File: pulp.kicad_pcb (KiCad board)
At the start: 2 copper layers, 25 parts, among them U2 RP2040, X2 ASE-12.0MHz

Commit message: made edits to PWM
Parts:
- added J1: Conn_01x03_Pin, Connector:FanPinHeader_1x03_P2.54mm_Vertical, F.Cu at (83.0, 79.9)
- moved R10 7.69 mm to (66.0, 99.7), turned to 90 degrees
- moved R11 4.09 mm to (70.3, 100.6)
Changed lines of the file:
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@@
   (net 51 "unconnected-(U2-GPIO29_ADC3-Pad41)")
   (net 52 "/RP2040.kicad_sch/QSPI_SS")
+  (net 53 "/3V3")
   (footprint "Resistor_SMD:R_0201_0603Metric" (layer "F.Cu")
     (at 63.59 71.91)
@@
   )
   (footprint "Resistor_SMD:R_0201_0603Metric" (layer "F.Cu")
-    (at 58.42 98.364 -90)
+    (at 66 99.655 90)
     (descr "Resistor SMD 0201 (0603 Metric), square (rectangular) end terminal, IPC_7351 nominal, (Body size source: https://www.vishay.com/docs/20052/crcw0201e3.pdf), generated with kicad-footprint-generator")
     (tags "resistor")
@@
     (fp_line (start 0.3 0.15) (end -0.3 0.15)
       (stroke (width 0.1) (type solid)) (layer "F.Fab"))
-    (pad "" smd roundrect (at -0.345 0 270) (size 0.318 0.36) (layers "F.Paste") (roundrect_rratio 0.25))
-    (pad "" smd roundrect (at 0.345 0 270) (size 0.318 0.36) (layers "F.Paste") (roundrect_rratio 0.25))
-    (pad "1" smd roundrect (at -0.32 0 270) (size 0.46 0.4) (layers "F.Cu" "F.Mask") (roundrect_rratio 0.25)
+    (pad "" smd roundrect (at -0.345 0 90) (size 0.318 0.36) (layers "F.Paste") (roundrect_rratio 0.25))
+    (pad "" smd roundrect (at 0.345 0 90) (size 0.318 0.36) (layers "F.Paste") (roundrect_rratio 0.25))
+    (pad "1" smd roundrect (at -0.32 0 90) (size 0.46 0.4) (layers "F.Cu" "F.Mask") (roundrect_rratio 0.25)
       (net 3 "/RP2040.kicad_sch/3V3") (pintype "passive"))
-    (pad "2" smd roundrect (at 0.32 0 270) (size 0.46 0.4) (layers "F.Cu" "F.Mask") (roundrect_rratio 0.25)
+    (pad "2" smd roundrect (at 0.32 0 90) (size 0.46 0.4) (layers "F.Cu" "F.Mask") (roundrect_rratio 0.25)
       (net 5 "Net-(X2-EN)") (pintype "passive"))
     (model "${KICAD6_3DMODEL_DIR}/Resistor_SMD.3dshapes/R_0201_0603Metric.wrl"
@@
   )
   (footprint "Resistor_SMD:R_0201_0603Metric" (layer "F.Cu")
-    (at 66.228 100.584)
+    (at 70.32 100.584)
     (descr "Resistor SMD 0201 (0603 Metric), square (rectangular) end terminal, IPC_7351 nominal, (Body size source: https://www.vishay.com/docs/20052/crcw0201e3.pdf), generated with kicad-footprint-generator")
     (tags "resistor")
@@
       (net 1 "/RP2040.kicad_sch/~{RST}") (pintype "passive"))
     (model "${KICAD6_3DMODEL_DIR}/Resistor_SMD.3dshapes/R_0201_0603Metric.wrl"
+      (offset (xyz 0 0 0))
+      (scale (xyz 1 1 1))
+      (rotate (xyz 0 0 0))
+    )
+  )
+  (footprint "Connector:FanPinHeader_1x03_P2.54mm_Vertical" (layer "F.Cu")
+    (at 83 79.92 -90)
+    (descr "3-pin CPU fan Through hole pin header, see http://www.formfactors.org/developer%5Cspecs%5Crev1_2_public.pdf")
+    (tags "pin header 3-pin CPU fan")
+    (property "Sheetfile" "pulp.kicad_sch")
+    (property "Sheetname" "")
+    (property "ki_description" "Generic connector, single row, 01x03, script generated")
+    (property "ki_keywords" "connector")
+    (attr through_hole)
+    (fp_text reference "J1" (at 2.5 -3.4 90) (layer "F.SilkS")
+        (effects (font (size 1 1) (thickness 0.15)))
+    )
+    (fp_text value "Conn_01x03_Pin" (at 2.55 4.5 90) (layer "F.Fab")
+        (effects (font (size 1 1) (thickness 0.15)))
+    )
+    (fp_text user "${REFERENCE}" (at 2.45 1.8 90) (layer "F.Fab")
+        (effects (font (size 1 1) (thickness 0.15)))
+    )
+    (fp_line (start -1.35 -2.65) (end 6.45 -2.65)
+      (stroke (width 0.12) (type solid)) (layer "F.SilkS"))
+    (fp_line (start -1.35 3.4) (end -1.35 -2.65)
+      (stroke (width 0.12) (type solid)) (layer "F.SilkS"))
+    (fp_line (start 0 2.29) (end 5.08 2.29)
+      (stroke (width 0.12) (type solid)) (layer "F.SilkS"))
+    (fp_line (start 0 3.3) (end 0 2.29)
+      (stroke (width 0.12) (type solid)) (layer "F.SilkS"))
+    (fp_line (start 5.08 2.29) (end 5.08 3.3)
+      (stroke (width 0.12) (type solid)) (layer "F.SilkS"))
+    (fp_line (start 6.45 -2.65) (end 6.45 3.4)
+      (stroke (width 0.12) (type solid)) (layer "F.SilkS"))
+    (fp_line (start 6.45 3.4) (end -1.35 3.4)
+      (stroke (width 0.12) (type solid)) (layer "F.SilkS"))
+    (fp_line (start -1.75 3.8) (end -1.75 -3.05)
+      (stroke (width 0.05) (type solid)) (layer "F.CrtYd"))
+    (fp_line (start -1.75 3.8) (end 6.85 3.8)
+      (stroke (width 0.05) (type solid)) (layer "F.CrtYd"))
+    (fp_line (start 6.85 -3.05) (end -1.75 -3.05)
+      (stroke (width 0.05) (type solid)) (layer "F.CrtYd"))
+    (fp_line (start 6.85 -3.05) (end 6.85 3.8)
+      (stroke (width 0.05) (type solid)) (layer "F.CrtYd"))
+    (fp_line (start -1.25 -2.55) (end 6.35 -2.55)
+      (stroke (width 0.1) (type solid)) (layer "F.Fab"))
+    (fp_line (start -1.25 3.3) (end -1.25 -2.55)
+      (stroke (width 0.1) (type solid)) (layer "F.Fab"))
+    (fp_line (start 0 2.3) (end 0 3.3)
+      (stroke (width 0.1) (type solid)) (layer "F.Fab"))
+    (fp_line (start 5.05 2.3) (end 0 2.3)
+      (stroke (width 0.1) (type solid)) (layer "F.Fab"))
+    (fp_line (start 5.05 3.3) (end 5.05 2.3)
+      (stroke (width 0.1) (type solid)) (layer "F.Fab"))
+    (fp_line (start 6.35 -2.55) (end 6.35 3.3)
+      (stroke (width 0.1) (type solid)) (layer "F.Fab"))
+    (fp_line (start 6.35 3.3) (end -1.25 3.3)
+      (stroke (width 0.1) (type solid)) (layer "F.Fab"))
+    (pad "1" thru_hole rect (at 0 0) (size 2.03 1.73) (drill 1.02) (layers "*.Cu" "*.Mask")
+      (net 32 "/RP2040.kicad_sch/GPIO14_PWM_RIGHT") (pinfunction "Pin_1") (pintype "passive"))
+    (pad "2" thru_hole oval (at 2.54 0) (size 2.03 1.73) (drill 1.02) (layers "*.Cu" "*.Mask")
+      (net 2 "GND") (pinfunction "Pin_2") (pintype "passive"))
+    (pad "3" thru_hole oval (at 5.08 0) (size 2.03 1.73) (drill 1.02) (layers "*.Cu" "*.Mask")
+      (net 53 "/3V3") (pinfunction "Pin_3") (pintype "passive"))
+    (model "${KICAD6_3DMODEL_DIR}/Connector.3dshapes/FanPinHeader_1x03_P2.54mm_Vertical.wrl"
       (offset (xyz 0 0 0))
       (scale (xyz 1 1 1))
@@
   (gr_rect (start 45.72 40.64) (end 86.36 121.92)
     (stroke (width 0.2) (type default)) (fill none) (layer "F.Cu"))
-  (segment (start 65.874 100.55) (end 65.908 100.584) (width 0.25) (layer "F.Cu") (net 3))
 )

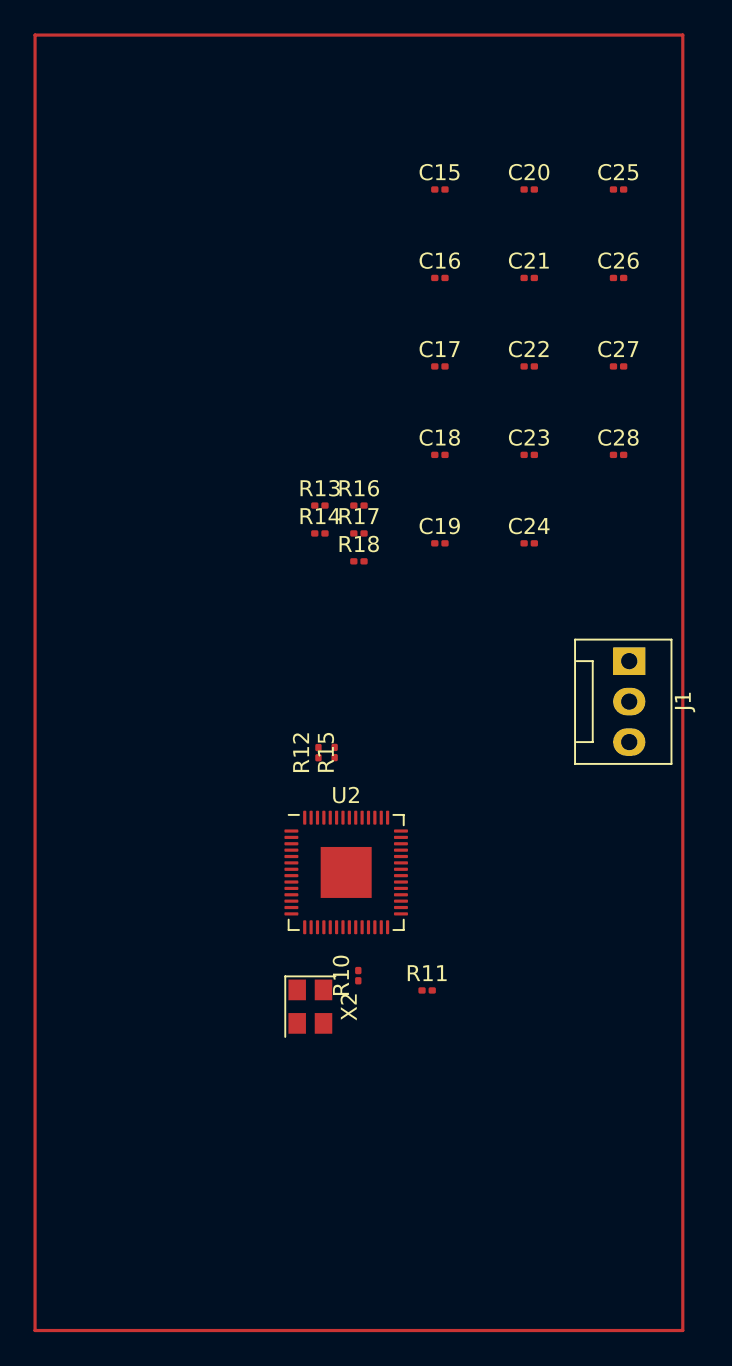
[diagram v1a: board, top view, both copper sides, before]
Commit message: adds QMC5883L
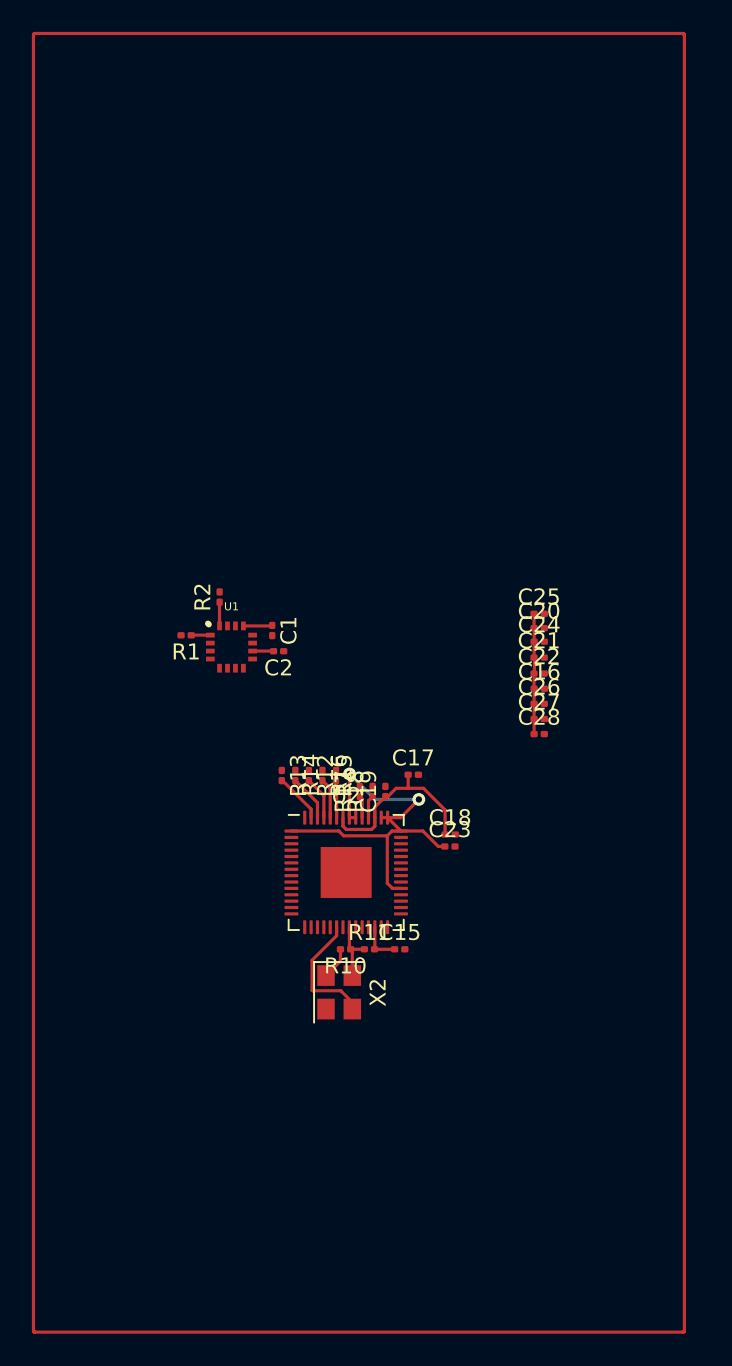
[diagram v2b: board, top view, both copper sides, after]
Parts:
- removed J1: Conn_01x03_Pin, Connector:FanPinHeader_1x03_P2.54mm_Vertical
- added C1: 0.1uF, Capacitor_SMD:C_0201_0603Metric, F.Cu at (60.6, 78.0)
- added C2: 4.7uF, Capacitor_SMD:C_0201_0603Metric, F.Cu at (61.0, 79.3)
- added R1: 4.7K, Resistor_SMD:R_0201_0603Metric, F.Cu at (55.2, 78.3)
- added R2: 4.7K, Resistor_SMD:R_0201_0603Metric, F.Cu at (57.3, 75.9)
- added U1: HMC5883L, Sensor:HMC5883L, F.Cu at (58.0, 79.0)
- moved C15 47.7 mm to (68.6, 98.0)
- moved C20 27.5 mm to (77.3, 77.8)
- moved C26 27.2 mm to (77.3, 82.6)
- moved C25 27.1 mm to (77.3, 77.0)
- moved C16 26.5 mm to (77.4, 81.7)
- moved C17 25.7 mm to (69.5, 87.0)
- moved C23 25.1 mm to (71.8, 91.5)
- moved C18 23.8 mm to (71.8, 90.8)
- moved C21 23.8 mm to (77.3, 79.7)
- moved C27 22.7 mm to (77.3, 83.5)
- moved C22 19.3 mm to (77.3, 80.7)
- moved C28 18.2 mm to (77.3, 84.5)
- moved R13 17.1 mm to (61.2, 87.1), turned to -90 degrees
- moved R16 17.1 mm to (63.8, 87.1), turned to -90 degrees
- moved R17 16.2 mm to (66.1, 88.1), turned to 90 degrees
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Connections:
- U2 pad 32: /RP2040.kicad_sch/I2C 0 SDA -> /QMC5883L/SDA
- U2 pad 34: /RP2040.kicad_sch/I2C 0 SCL -> /QMC5883L/SCL
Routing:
- net /RP2040.kicad_sch/3V3: track 0.00 -> 38.0 mm, vias 0 -> 2
- net /RP2040.kicad_sch/1V1: track 0.00 -> 11.8 mm
- net Net-(U2-XIN): track 0.00 -> 7.86 mm
- net Net-(U2-QSPI_SD1): track 0.00 -> 3.11 mm
- net Net-(U2-QSPI_SD2): track 0.00 -> 2.90 mm
- net Net-(U2-QSPI_SD0): track 0.00 -> 2.71 mm
- net /RP2040.kicad_sch/~{RST}: track 0.00 -> 2.65 mm
- net Net-(U2-QSPI_SCLK): track 0.00 -> 2.53 mm
- net Net-(U2-QSPI_SD3): track 0.00 -> 2.34 mm
- net Net-(X2-EN): track 0.00 -> 2.02 mm
- net /QMC5883L/3V3: track 0.00 -> 1.82 mm
- net /QMC5883L/SDA: track 0.00 -> 1.50 mm
- net /RP2040.kicad_sch/USB_D+: track 0.00 -> 1.43 mm
- net /RP2040.kicad_sch/USB_D-: track 0.00 -> 1.38 mm
- net Net-(U1-C1): track 0.00 -> 1.32 mm
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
